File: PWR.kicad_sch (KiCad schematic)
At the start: 41 parts, among them J1 USB_B_Mini, J15 Conn_01x02_Pin, J2 Conn_01x03_Pin, J3 Conn_01x03_Pin, J7 Conn_01x02_Pin, Q1 AO3400A, Q2 AO3400A, U10 SRV05-4, U5 AMS1117-3.3

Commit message: feat: расположены основные узлы модуля на печатной плате
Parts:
- added F2: MF-MSMF110-2, Fuse:Fuse_1812_4532Metric_Pad1.30x3.40mm_HandSolder, symbol FUSE:MF-MSMF110-2
- renumbered C12 to C1, C9 to C10, C47 to C11, C36 to C12, C46 to C13, C7 to C2, C8 to C3, C1 to C4, C2 to C5, C3 to C6, C4 to C7, C5 to C8, C6 to C9, D3 to D2, D9 to D3, D15 to D4, D2 to D5, D20 to D6, D5 to D7, D4 to D8, J15 to J4, J7 to J5, Q2 to Q1, Q1 to Q2, R47 to R1, R15 to R2, R27 to R3, R13 to R4, R46 to R5, R24 to R6, R30 to R7, R45 to R8, R26 to R9, U5 to U1, U10 to U2, VD6 to VD1
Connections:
- net +5V_in: no longer C10.1, C8.1, C9.1, D5.2 (A), D6.2 (A2), J2.1 (Pin_1)
- new net: C10.1, C8.1, C9.1, D5.2 (A), D6.2 (A2), F2.2 (A2)
- new net: F2.1 (A1), J2.1 (Pin_1)
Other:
- moved on the sheet: C10, C8, C9, D5, D6

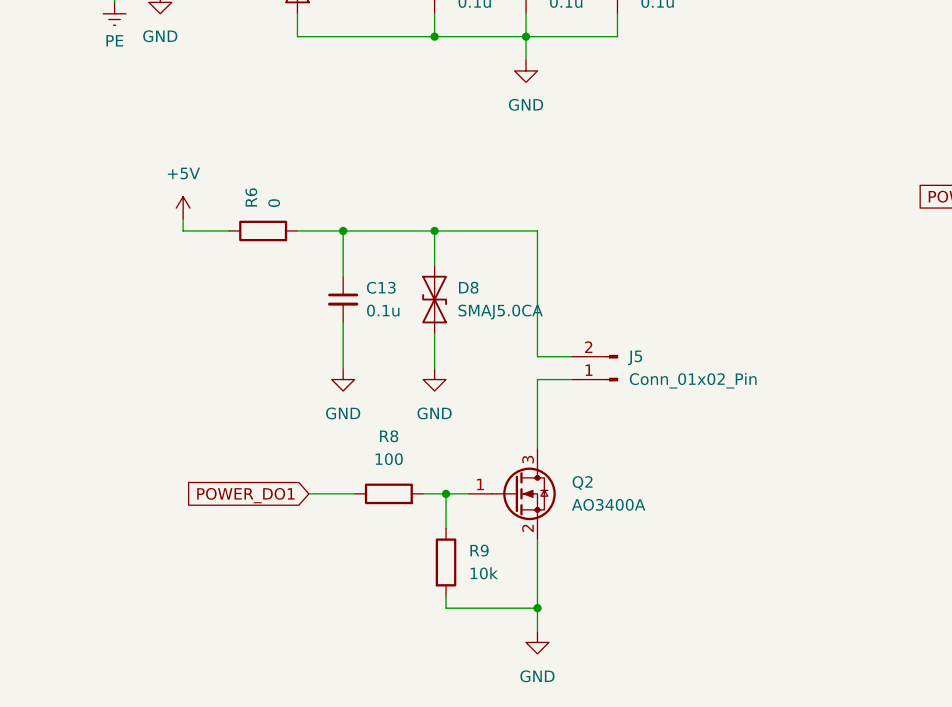
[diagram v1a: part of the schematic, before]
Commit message: feat: добавлена обвязка внешних интерфейсов
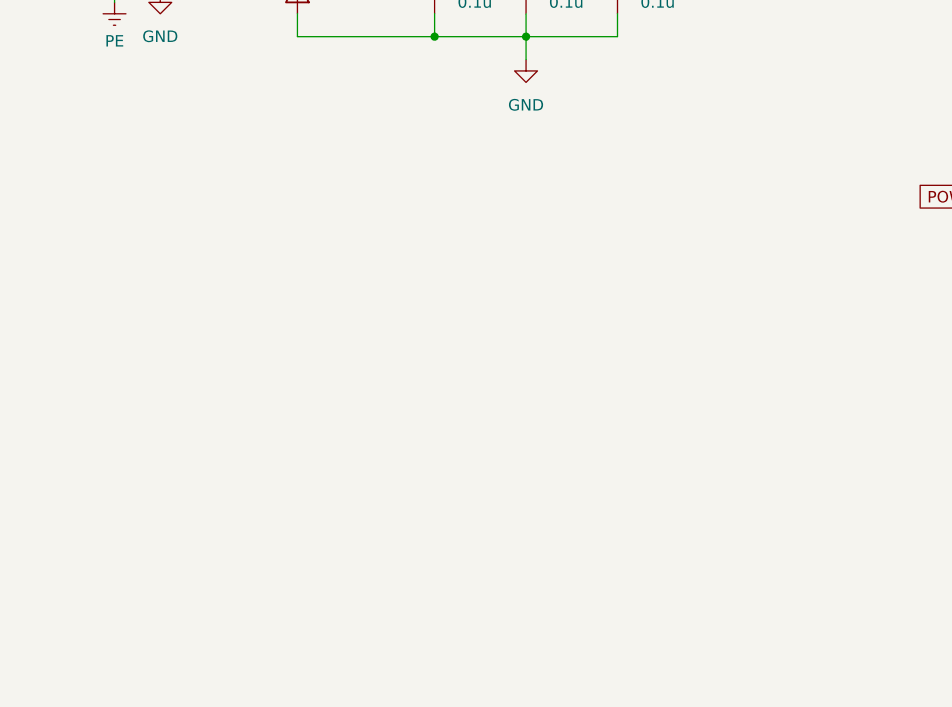
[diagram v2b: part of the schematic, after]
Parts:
- removed C13: 0.1u, Capacitor_SMD:C_0805_2012Metric_Pad1.18x1.45mm_HandSolder, symbol Device:C_Small
- removed D8: SMAJ5.0CA, Diode_SMD:D_SMA, symbol Diode:SMAJ5.0CA
- removed J5: Conn_01x02_Pin, Connector_PinHeader_2.54mm:PinHeader_1x02_P2.54mm_Vertical, symbol Connector:Conn_01x02_Pin
- removed Q2: AO3400A, Package_TO_SOT_SMD:SOT-23, symbol Transistor_FET:AO3400A
- removed R6: 0, Resistor_SMD:R_0805_2012Metric_Pad1.20x1.40mm_HandSolder, symbol Device:R
- removed R8: 100, Resistor_SMD:R_0805_2012Metric_Pad1.20x1.40mm_HandSolder, symbol Device:R
- removed R9: 10k, Resistor_SMD:R_0805_2012Metric_Pad1.20x1.40mm_HandSolder, symbol Device:R
